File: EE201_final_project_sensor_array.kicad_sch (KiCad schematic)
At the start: 16 parts, among them J1 Conn_01x07_Pin, J2 Conn_01x02_Pin

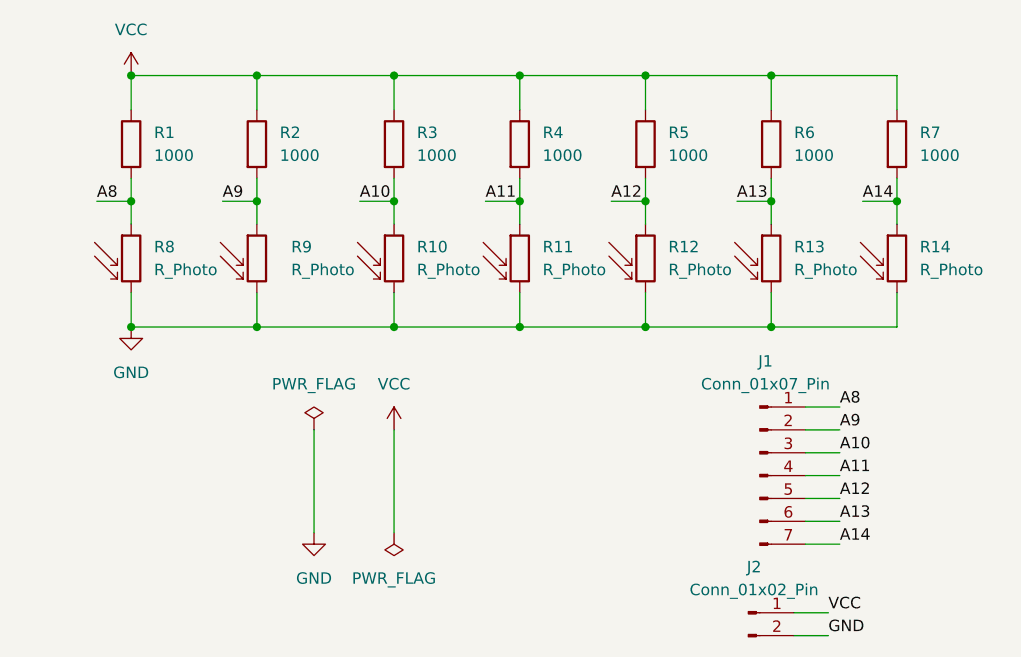
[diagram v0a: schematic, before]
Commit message: Changed  to include optional shield excercise
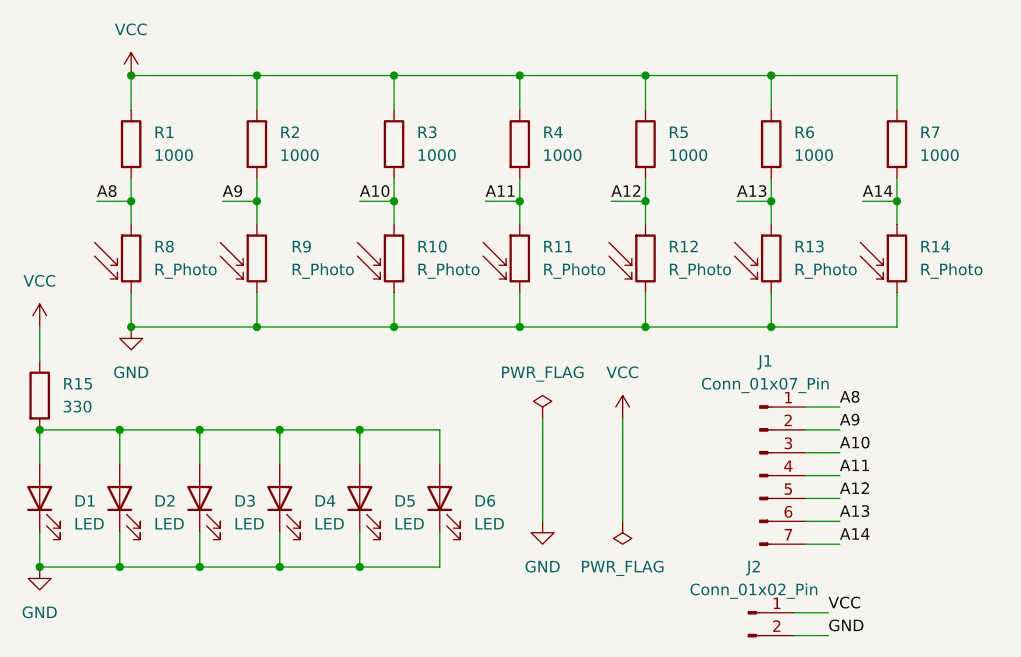
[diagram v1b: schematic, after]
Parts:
- added D1, D2, D3, D4, D5, D6: LED, symbol Device:LED
- added R15: 330, symbol Device:R
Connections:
- net GND: now also D1.1 (K), D2.1 (K), D3.1 (K), D4.1 (K), D5.1 (K), D6.1 (K)
- net VCC: now also R15.1
- new net: D1.2 (A), D2.2 (A), D3.2 (A), D4.2 (A), D5.2 (A), D6.2 (A), R15.2
